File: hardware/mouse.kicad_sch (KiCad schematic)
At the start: 58 parts, among them J2 JSTPH, J3 USB_C_Receptacle_USB2.0_14P, SW1 SW_SPST, SW2 SW_SPST, SW3 SW_SPST, SW4 SW_SPST, SW5 SW_SPST, SW6 SW_SPST, SW7 RotaryEncoder, SW7 SW_SPST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

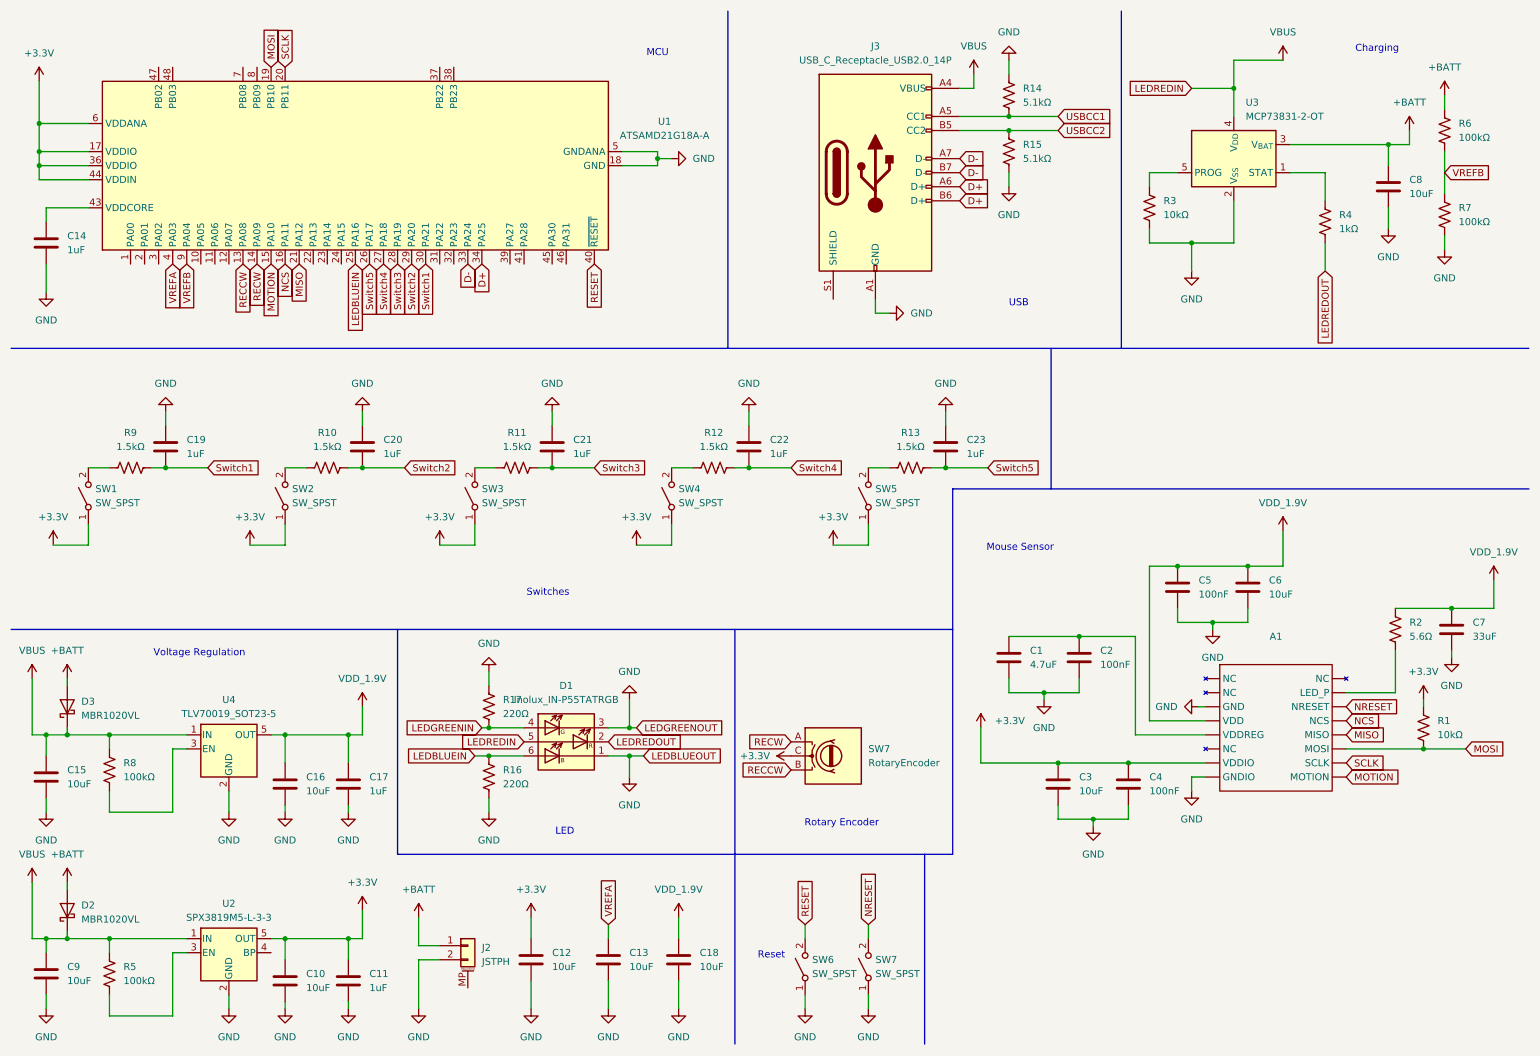
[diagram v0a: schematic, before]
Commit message: finished schem, peer review next
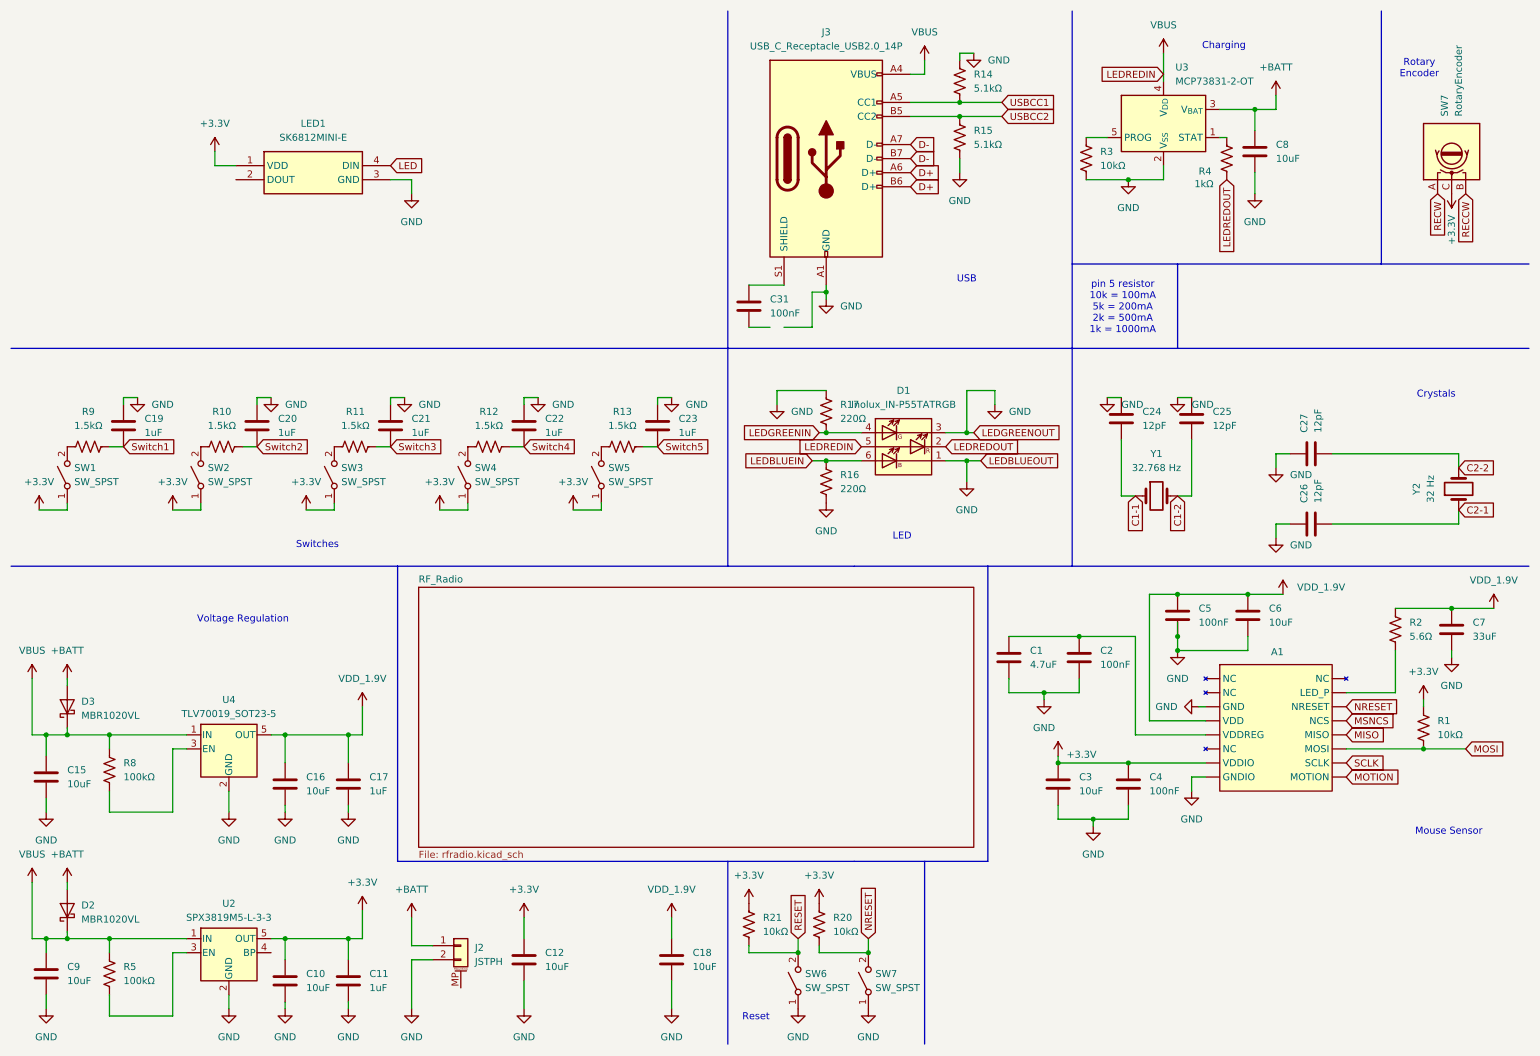
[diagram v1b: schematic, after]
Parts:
- removed C13: 10uF, symbol Device:C
- removed C14: 1uF, symbol Device:C
- removed R6, R7: 100kΩ, symbol Device:R_US
- removed U1: ATSAMD21G18A-A, Package_QFP:TQFP-48_7x7mm_P0.5mm, symbol MCU_Microchip_SAMD:ATSAMD21G18A-A
- added C24, C25, C26, C27: 12pF, symbol Device:C
- added C31: 100nF, symbol Device:C
- added LED1: SK6812MINI-E, SK6812MINIE, symbol Custom:SK6812MINI-E
- added R20, R21: 10kΩ, symbol Device:R_US
- added Y1: 32.768 Hz, symbol Device:Crystal
- added Y2: 32 Hz, symbol Device:Crystal
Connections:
- net NCS is gone; now on net VDD_1.9V: A1. (MOTION)
- net +3.3V: now also LED1.1 (VDD), R20.2, R21.2
- net GND: now also C24.1, C25.1, C26.1, C27.1, LED1.3 (GND)
- net NRESET: now also R20.1
- net RESET: now also R21.1
- net at J3.S1 (SHIELD): now also C31.1
- new net C1-1: C24.2, Y1.1
- new net C1-2: C25.2, Y1.2
- new net C2-1: C26.2, Y2.1
- new net C2-2: C27.2, Y2.2
- new net LED: LED1.4 (DIN)
- new net MSNCS: A1. (MOTION)
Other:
- added sheet RF_Radio (rfradio.kicad_sch)
- note added: "Crystals"
- note added: "pin 5 resistor 10k = 100mA 5k = 200mA 2k = 500mA 1k = 1000mA"
- note removed: "MCU"
- moved on the sheet: C12, C18, C19, C20, C21, C22, C23, C5, C6, C8, D1, J2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
